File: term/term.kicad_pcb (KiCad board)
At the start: 2 copper layers, 35.6 x 30.5 mm, 23 parts, among them P101 CONN_01X08, P102 XG4C-1631, P103 CONN_01X08, SW101 SW_PUSH

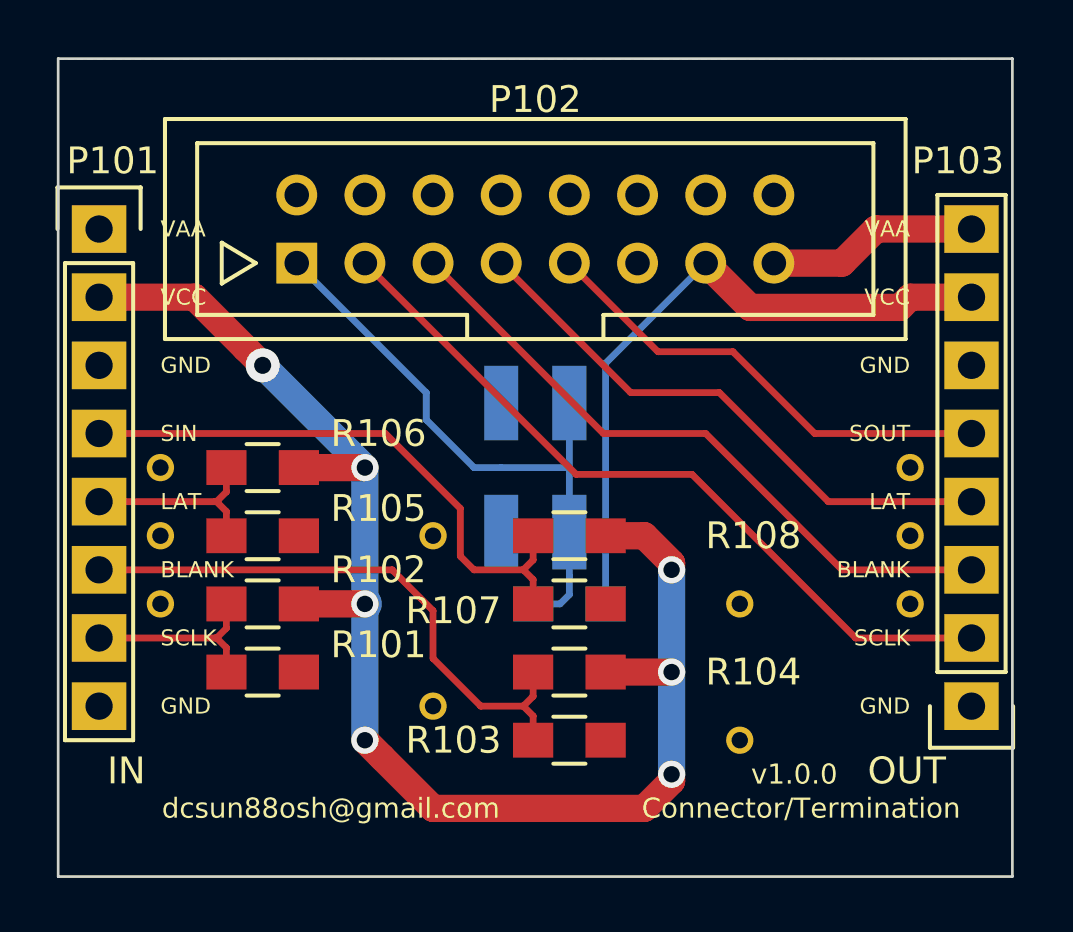
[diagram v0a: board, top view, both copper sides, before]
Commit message: Add wire pads for display power. Generate gerbers for termination board. Upload to OSHPark.
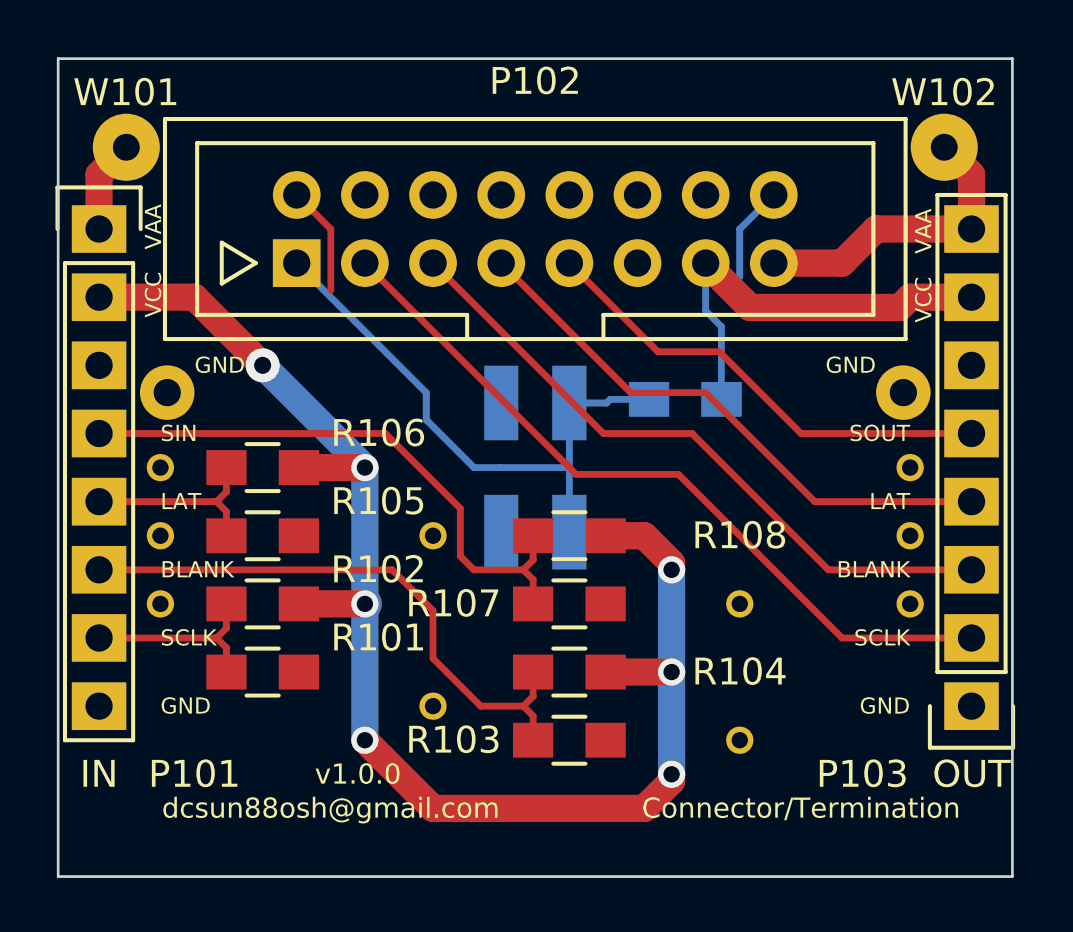
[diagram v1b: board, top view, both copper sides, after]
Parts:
- added REF**: Stitching_Via_40x24mil, local:Stitching_Via_40x24mil, F.Cu at (158.5, 96.3)
- added REF**: Stitching_Via_40x24mil, local:Stitching_Via_40x24mil, F.Cu at (131.1, 96.3)
- added W101: TEST_1P, Wire_Pads:SolderWirePad_single_1mmDrill, F.Cu at (129.5, 87.1)
- added W102: TEST_1P, Wire_Pads:SolderWirePad_single_1mmDrill, F.Cu at (160.0, 87.1)
- moved R109 8.76 mm to (150.4, 96.5)
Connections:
- net Net-(P102-Pad13) renamed /VCC_IN
- net Net-(P102-Pad15) renamed /VAA_IN
- P101 pad 1: (no net) -> VAA
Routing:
- net /VCC_IN: track 25.0 -> 16.1 mm
- net GND: track 0.00 -> 7.66 mm
- net /VAA_IN: track 7.89 -> 11.4 mm
- net VAA: track 0.00 -> 3.47 mm
- net /~RESET~: track 22.5 -> 21.7 mm

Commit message: New version of the termination/connector board. Add LED indicators for status and power.
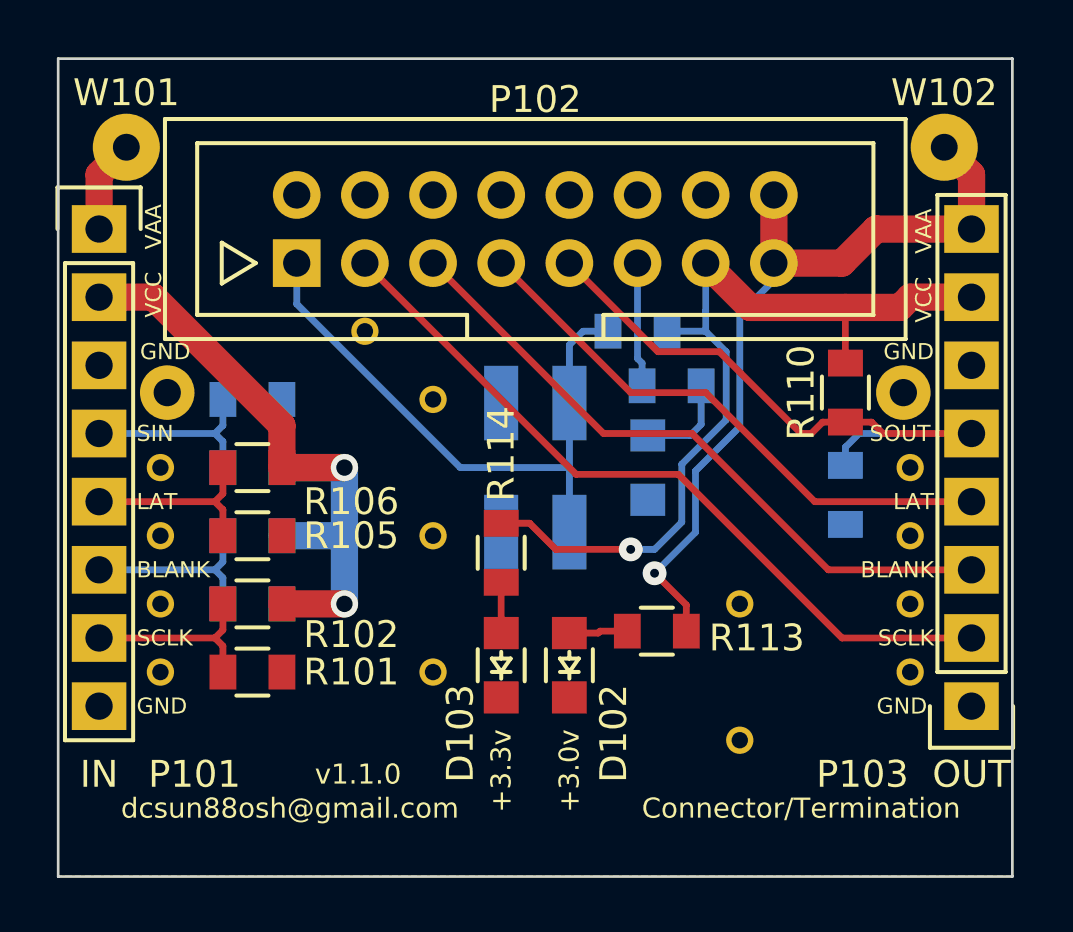
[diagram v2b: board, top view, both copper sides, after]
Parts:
- added D101: RED, local:LED_0805_HandSoldering, B.Cu at (149.0, 99.1)
- added D102: GREEN, local:LED_0805_HandSoldering, F.Cu at (146.1, 106.4)
- added D103: GREEN, local:LED_0805_HandSoldering, F.Cu at (143.5, 106.4)
- added R110: 210R, local:R_0805_HandSoldering, F.Cu at (156.3, 96.3)
- added R111: 210R, local:R_0805_HandSoldering, B.Cu at (156.3, 100.1)
- added R112: 1K, local:R_0805_HandSoldering, B.Cu at (149.9, 96.0)
- added R113: 1K, local:R_0805_HandSoldering, F.Cu at (149.3, 105.2)
- added R114: 1K, local:R_0805_HandSoldering, F.Cu at (143.5, 102.2)
- added REF**: Stitching_Via_40x24mil, local:Stitching_Via_40x24mil, F.Cu at (138.4, 94.0)
- added REF**: Stitching_Via_40x24mil, local:Stitching_Via_40x24mil, F.Cu at (141.0, 96.5)
- added REF**: Stitching_Via_40x24mil, local:Stitching_Via_40x24mil, F.Cu at (158.8, 106.7)
- added REF**: Stitching_Via_40x24mil, local:Stitching_Via_40x24mil, F.Cu at (130.8, 106.7)
- R101, R102, R105, R106, R109: footprint Resistors_SMD:R_0805_HandSoldering -> local:R_0805_HandSoldering
- R103, R104, R107, R108: footprint Resistors_SMD:R_0805_HandSoldering -> local:R_0805_HandSoldering; moved to B.Cu
- moved R107 14.1 mm to (134.2, 96.5)
- moved R104 12.9 mm to (134.2, 101.6)
- moved R103 12.9 mm to (134.2, 104.1)
- moved R108 12.1 mm to (134.2, 99.1)
- moved R109 3.10 mm to (148.6, 94.0)
- moved REF** 1.27 mm to (141.0, 106.7)
- moved R101 0.38 mm to (134.2, 106.7)
- moved R102 0.38 mm to (134.2, 104.1)
- moved R105 0.38 mm to (134.2, 101.6)
- moved R106 0.38 mm to (134.2, 99.1)
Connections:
- net Net-(P101-Pad5) renamed /LAT_TERM
- net Net-(P101-Pad6) renamed /BLANK_TERM
- net Net-(P101-Pad7) renamed /SCLK_TERM
- P102 pad 11: GND -> /STATUS
- P102 pad 16: GND -> /VAA_IN
- P102 pad 2: GND -> Net-(P102-Pad2)
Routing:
- net VCC: track 54.1 -> 24.8 mm, vias 7 -> 2
- net /VAA_IN: track 11.4 -> 29.9 mm, vias 0 -> 1
- net /VCC_IN: track 16.1 -> 32.5 mm, vias 0 -> 1
- net /SIN: track 21.8 -> 7.10 mm
- net /BLANK_TERM: track 21.8 -> 7.10 mm
- net GND: track 7.66 -> 0.00 mm
- net /SOUT: track 17.6 -> 23.6 mm
- net /STATUS: track 0.00 -> 4.64 mm
- net Net-(D101-Pad2): track 0.00 -> 3.60 mm
- net Net-(D102-Pad2): track 0.00 -> 2.19 mm
- net Net-(D103-Pad2): track 0.00 -> 1.89 mm
- net /~RESET~: track 21.7 -> 22.8 mm
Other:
- board text added: "+3.0v"
- board text added: "+3.3v"
- board text added: "v1.1.0"
- board text removed: "v1.0.0"

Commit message: Termination board:   Use power symbols from local library.   Generate gerbers.   Generate pdf schematic.   Generate BOM.
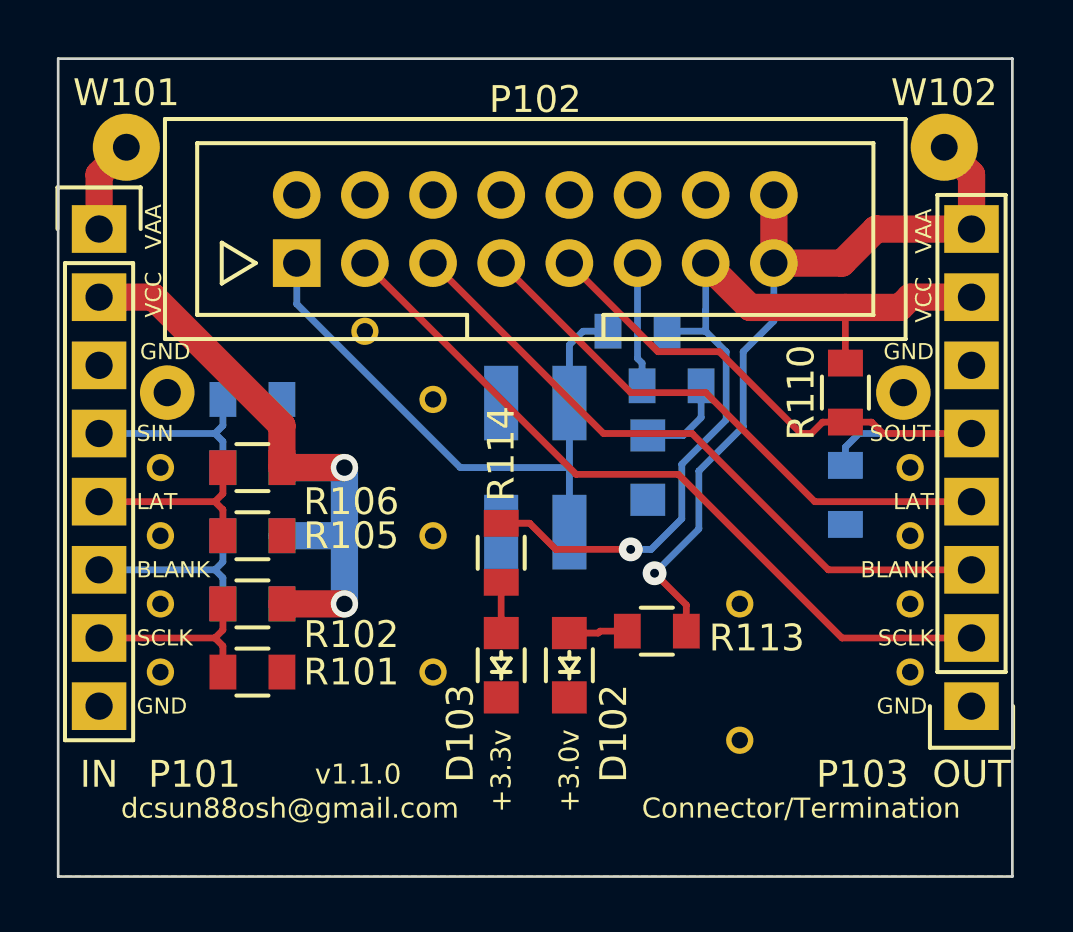
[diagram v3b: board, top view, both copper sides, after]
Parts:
- R112: value 1K -> 536
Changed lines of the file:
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@@
       (effects (font (size 1 1) (thickness 0.15)) (justify mirror))
     )
-    (fp_text value 1K (at 0 -2.1) (layer B.Fab)
+    (fp_text value 536 (at 0 -2.1) (layer B.Fab)
       (effects (font (size 1 1) (thickness 0.15)) (justify mirror))
     )
@@
   (segment (start 146.05 101.465) (end 146.05 99.06) (width 0.254) (layer B.Cu) (net 8))
   (segment (start 146.05 99.06) (end 146.05 96.655) (width 0.254) (layer B.Cu) (net 8))
+  (segment (start 148.336 102.108) (end 149.098 102.108) (width 0.254) (layer B.Cu) (net 9))
+  (segment (start 149.098 102.108) (end 150.241 100.965) (width 0.254) (layer B.Cu) (net 9))
+  (segment (start 150.241 100.965) (end 150.241 98.933) (width 0.254) (layer B.Cu) (net 9))
+  (segment (start 150.241 98.933) (end 151.892 97.282) (width 0.254) (layer B.Cu) (net 9))
+  (segment (start 151.892 97.282) (end 151.892 94.742) (width 0.254) (layer B.Cu) (net 9))
+  (segment (start 151.892 94.742) (end 151.13 93.98) (width 0.254) (layer B.Cu) (net 9))
   (segment (start 148.336 102.108) (end 145.542 102.108) (width 0.254) (layer F.Cu) (net 9))
   (segment (start 145.542 102.108) (end 144.569 101.135) (width 0.254) (layer F.Cu) (net 9))
   (segment (start 144.569 101.135) (end 143.51 101.135) (width 0.254) (layer F.Cu) (net 9))
-  (segment (start 148.336 102.108) (end 149.225 102.108) (width 0.254) (layer B.Cu) (net 9))
-  (segment (start 149.225 102.108) (end 150.241 101.092) (width 0.254) (layer B.Cu) (net 9))
-  (segment (start 150.241 101.092) (end 150.241 98.933) (width 0.254) (layer B.Cu) (net 9))
-  (segment (start 150.241 98.933) (end 151.892 97.282) (width 0.254) (layer B.Cu) (net 9))
-  (segment (start 151.892 97.282) (end 151.892 94.742) (width 0.254) (layer B.Cu) (net 9))
-  (segment (start 151.892 94.742) (end 151.13 93.98) (width 0.254) (layer B.Cu) (net 9))
   (via (at 148.336 102.108) (size 0.889) (drill 0.3302) (layers F.Cu B.Cu) (net 9))
   (segment (start 151.13 93.98) (end 151.13 93.218) (width 0.254) (layer B.Cu) (net 9))
@@
   (segment (start 158.75 92.71) (end 161.036 92.71) (width 1.016) (layer F.Cu) (net 9))
   (segment (start 158.368999 93.091001) (end 158.75 92.71) (width 1.016) (layer F.Cu) (net 9))
+  (segment (start 149.225 102.997) (end 150.876 101.346) (width 0.254) (layer B.Cu) (net 10))
+  (segment (start 150.876 101.346) (end 150.876 99.187) (width 0.254) (layer B.Cu) (net 10))
+  (segment (start 150.876 99.187) (end 152.527 97.536) (width 0.254) (layer B.Cu) (net 10))
+  (segment (start 152.527 97.536) (end 152.527 94.742) (width 0.254) (layer B.Cu) (net 10))
+  (segment (start 152.527 94.742) (end 153.67 93.599) (width 0.254) (layer B.Cu) (net 10))
+  (segment (start 153.67 93.599) (end 153.67 91.44) (width 0.254) (layer B.Cu) (net 10))
   (segment (start 149.225 102.997) (end 150.409 104.181) (width 0.254) (layer F.Cu) (net 10))
   (segment (start 150.409 104.181) (end 150.409 105.156) (width 0.254) (layer F.Cu) (net 10))
   (via (at 149.225 102.997) (size 0.889) (drill 0.3302) (layers F.Cu B.Cu) (net 10))
-  (segment (start 149.225 102.997) (end 150.749 101.473) (width 0.254) (layer B.Cu) (net 10))
-  (segment (start 150.749 101.473) (end 150.749 99.187) (width 0.254) (layer B.Cu) (net 10))
-  (segment (start 150.749 99.187) (end 152.4 97.536) (width 0.254) (layer B.Cu) (net 10))
-  (segment (start 152.4 97.536) (end 152.4 93.345) (width 0.254) (layer B.Cu) (net 10))
-  (segment (start 152.4 93.345) (end 153.67 92.075) (width 0.254) (layer B.Cu) (net 10))
-  (segment (start 153.67 92.075) (end 153.67 91.44) (width 0.254) (layer B.Cu) (net 10))
   (segment (start 153.67 91.44) (end 153.67 88.9) (width 1.016) (layer F.Cu) (net 10))
   (segment (start 161.036 90.17) (end 161.036 88.138) (width 1.016) (layer F.Cu) (net 10))
@@
   (segment (start 128.524 90.17) (end 128.524 88.138) (width 1.016) (layer F.Cu) (net 11))
   (segment (start 128.524 88.138) (end 129.54 87.122) (width 1.016) (layer F.Cu) (net 11))
-  (segment (start 150.96 97.452) (end 150.552 97.86) (width 0.254) (layer B.Cu) (net 13))
-  (segment (start 150.552 97.86) (end 148.971 97.86) (width 0.254) (layer B.Cu) (net 13))
-  (segment (start 150.96 96.012) (end 150.96 97.452) (width 0.254) (layer B.Cu) (net 13))
+  (segment (start 150.96 96.012) (end 150.96 97.198) (width 0.254) (layer B.Cu) (net 13))
+  (segment (start 150.96 97.198) (end 150.298 97.86) (width 0.254) (layer B.Cu) (net 13))
+  (segment (start 150.298 97.86) (end 148.971 97.86) (width 0.254) (layer B.Cu) (net 13))
   (segment (start 146.05 105.226) (end 147.123 105.226) (width 0.254) (layer F.Cu) (net 14))
   (segment (start 147.123 105.226) (end 147.193 105.156) (width 0.254) (layer F.Cu) (net 14))
